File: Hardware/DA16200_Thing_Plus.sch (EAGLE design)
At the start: 63 parts, among them J2 THING_PLUS, J3 Qwiic, J5 USB C, J6 microSD, J7 CORTEX_JTAG_DEBUG_PTH_NS, Q1 20V/4.2A/52mΩ/1.4W, U1 DA16200MOD, U2 CH340E_MSOP10, U3 MCP73831, U5 4MB Flash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

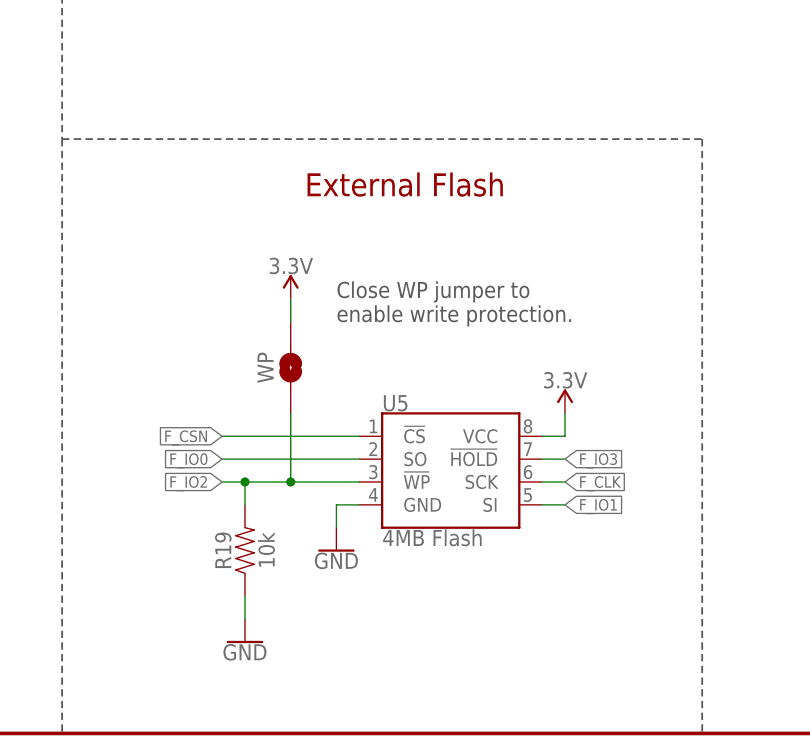
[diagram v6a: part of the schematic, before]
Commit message: Add "DNP" to external QSPI flash circuitry
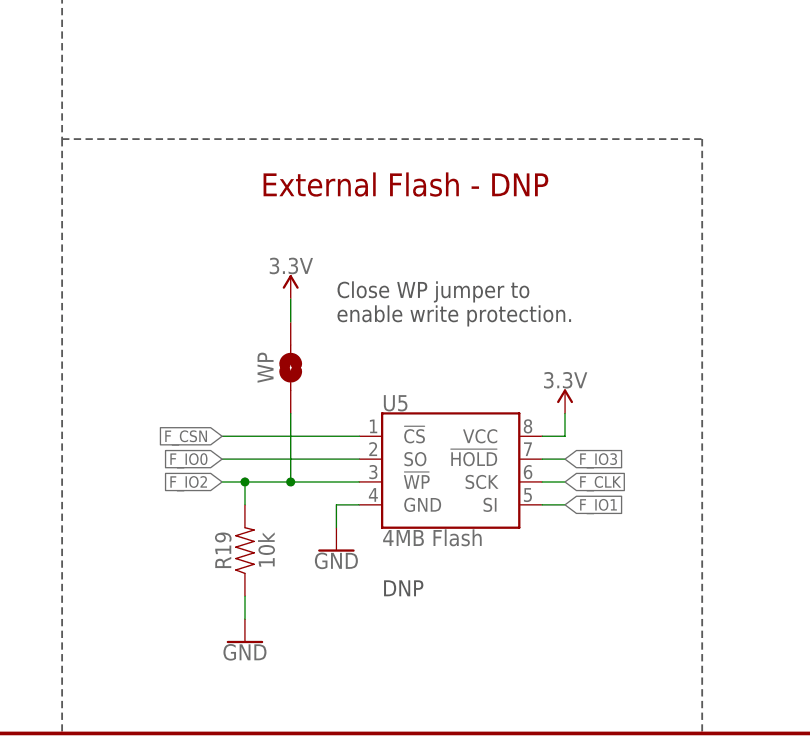
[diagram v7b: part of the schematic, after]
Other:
- note added: "DNP"
- note added: "External Flash - DNP"
- note removed: "External Flash"
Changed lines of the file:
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@@
 <wire x1="76.2" y1="66.04" x2="147.32" y2="66.04" width="0.2032" layer="97" style="longdash"/>
 <wire x1="147.32" y1="66.04" x2="147.32" y2="0" width="0.2032" layer="97" style="longdash"/>
-<text x="114.3" y="60.96" size="2.54" layer="94" font="vector" align="center">External Flash</text>
+<text x="114.3" y="60.96" size="2.54" layer="94" font="vector" align="center">External Flash - DNP</text>
 <text x="223.52" y="223.52" size="2.032" layer="97" font="vector" rot="MR0" align="top-right">Cut and resolder
 CHG jumper to
@@
 to remove LED
 from power.</text>
+<text x="111.76" y="15.24" size="1.778" layer="97" font="vector">DNP</text>
 </plain>
 <instances>

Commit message: Updates for Red's
* Added a NC jumper on the RTC_PWR_KEY pin to default to 3.3V. Users can cut the jumper to enter into sleep mode 1
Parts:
- removed R9: DNP, SparkFun-Resistors:DNP-0402T
- added RTC_PWR: JUMPER-SMT_2_NC_TRACE_SILK, SparkFun-Jumpers:JUMPER-SMT_2_NC_TRACE_SILK
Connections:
- net 3.3V: now also RTC_PWR.2; no longer R9.1
- net RTC_PWR_KEY: now also RTC_PWR.1; no longer R9.2
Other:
- note added: "The RTC_PWR_KEY pin enables the RTC block. Keep this pin connected to 3.3V for normal operation. Cut this jumper to enter sleep mode 1. Refer to the datasheet for more information."
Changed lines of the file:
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@@
 <part name="R5" library="SparkFun-Resistors" deviceset="4.7KOHM" device="-0402T-1/16W-1%" value="4.7k"/>
 <part name="R7" library="SparkFun-Resistors" deviceset="4.7KOHM" device="-0402T-1/16W-1%" value="4.7k"/>
-<part name="R9" library="SparkFun-Resistors" deviceset="DNP" device="-0402T" value="DNP"/>
 <part name="C3" library="SparkFun-Capacitors" deviceset="DNP" device="-0402-TIGHT" value="DNP"/>
 <part name="GND17" library="SparkFun-PowerSymbols" deviceset="GND" device=""/>
@@
 <part name="TMS" library="SparkFun-Connectors" deviceset="TEST-POINT" device="3"/>
 <part name="GPIOC7" library="SparkFun-Connectors" deviceset="TEST-POINT" device="3"/>
+<part name="RTC_PWR" library="SparkFun-Jumpers" deviceset="JUMPER-SMT_2_NC_TRACE" device="_SILK" package3d_urn="urn:adsk.eagle:package:39281/1"/>
 </parts>
 <sheets>
@@
 from power.</text>
 <text x="111.76" y="15.24" size="1.778" layer="97" font="vector">DNP</text>
+<text x="81.28" y="144.78" size="1.778" layer="97" font="vector">The RTC_PWR_KEY pin enables the
+RTC block. Keep this pin connected
+to 3.3V for normal operation. Cut this
+jumper to enter sleep mode 1. Refer
+to the datasheet for more information.</text>
 </plain>
 <instances>
@@
 <attribute name="VALUE" x="151.384" y="109.22" size="1.778" layer="96" font="vector" rot="R90" align="top-center"/>
 </instance>
-<instance part="R9" gate="G$1" x="142.24" y="134.62" smashed="yes" rot="R270">
-<attribute name="NAME" x="143.764" y="134.62" size="1.778" layer="95" font="vector" rot="R270" align="bottom-center"/>
-<attribute name="VALUE" x="140.716" y="134.62" size="1.778" layer="96" font="vector" rot="R270" align="top-center"/>
-</instance>
 <instance part="C3" gate="G$1" x="132.08" y="109.22" smashed="yes">
 <attribute name="NAME" x="133.604" y="112.141" size="1.778" layer="95" font="vector"/>
@@
 <instance part="GPIOC7" gate="G$1" x="312.42" y="157.48" smashed="yes" rot="R270">
 <attribute name="NAME" x="312.42" y="152.4" size="1.778" layer="95" font="vector" rot="R270"/>
+</instance>
+<instance part="RTC_PWR" gate="G$1" x="142.24" y="134.62" smashed="yes" rot="R90">
+<attribute name="NAME" x="139.192" y="134.62" size="1.778" layer="95" font="vector" rot="R90" align="center"/>
 </instance>
 </instances>
@@
 </segment>
 <segment>
-<pinref part="R9" gate="G$1" pin="1"/>
-<pinref part="SUPPLY8" gate="G$1" pin="3.3V"/>
-<wire x1="142.24" y1="142.24" x2="142.24" y2="139.7" width="0.1524" layer="91"/>
-</segment>
-<segment>
 <pinref part="SUPPLY36" gate="G$1" pin="3.3V"/>
 <pinref part="LED" gate="G$1" pin="2"/>
@@
 <pinref part="SUPPLY19" gate="G$1" pin="3.3V"/>
 <wire x1="226.06" y1="127" x2="226.06" y2="124.46" width="0.1524" layer="91"/>
+</segment>
+<segment>
+<pinref part="RTC_PWR" gate="G$1" pin="2"/>
+<pinref part="SUPPLY8" gate="G$1" pin="3.3V"/>
+<wire x1="142.24" y1="142.24" x2="142.24" y2="139.7" width="0.1524" layer="91"/>
 </segment>
 </net>
@@
 <pinref part="U1" gate="G$1" pin="RTC_PWR_KEY"/>
 <wire x1="167.64" y1="127" x2="142.24" y2="127" width="0.1524" layer="91"/>
-<pinref part="R9" gate="G$1" pin="2"/>
 <wire x1="142.24" y1="127" x2="132.08" y2="127" width="0.1524" layer="91"/>
 <wire x1="132.08" y1="127" x2="129.54" y2="127" width="0.1524" layer="91"/>
-<wire x1="142.24" y1="129.54" x2="142.24" y2="127" width="0.1524" layer="91"/>
-<junction x="142.24" y="127"/>
 <label x="129.54" y="127" size="1.27" layer="95" rot="R180" xref="yes"/>
 <pinref part="C3" gate="G$1" pin="1"/>
 <wire x1="132.08" y1="114.3" x2="132.08" y2="127" width="0.1524" layer="91"/>
 <junction x="132.08" y="127"/>
-</segment>
-<segment>
+<pinref part="RTC_PWR" gate="G$1" pin="1"/>
+<wire x1="142.24" y1="129.54" x2="142.24" y2="127" width="0.1524" layer="91"/>
+<junction x="142.24" y="127"/>
+</segment>
+<segment>
